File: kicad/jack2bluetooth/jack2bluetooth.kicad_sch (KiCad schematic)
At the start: 1 part, among them IC7 ESP32-WROVER-E-N16R8

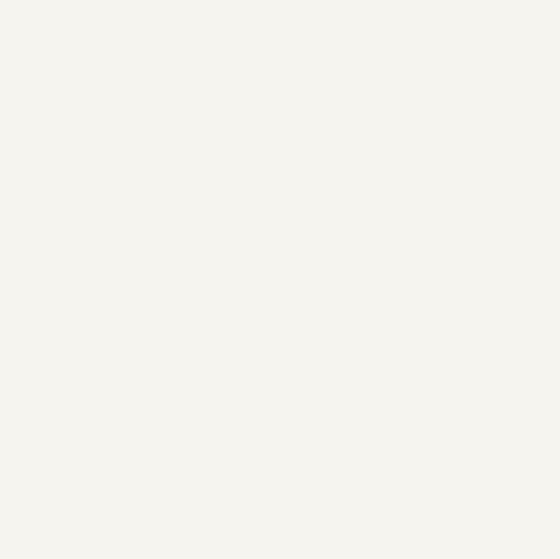
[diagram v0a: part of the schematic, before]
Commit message: doc: update datasheets
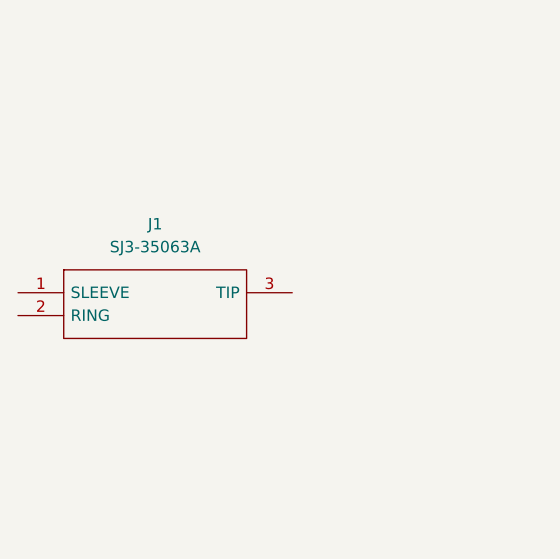
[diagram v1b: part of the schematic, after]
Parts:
- added J1: SJ3-35063A, SJ335063A, symbol SJ3-35063A:SJ3-35063A
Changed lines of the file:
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@@
+		)
+	)
+	(symbol
+		(lib_id "SJ3-35063A:SJ3-35063A")
+		(at 78.74 127 0)
+		(unit 1)
+		(exclude_from_sim no)
+		(in_bom yes)
+		(on_board yes)
+		(dnp no)
+		(fields_autoplaced yes)
+		(property "Reference" "J1"
+			(at 93.98 119.38 0)
+			(effects
+				(font
+					(size 1.27 1.27)
+				)
+			)
+		)
+		(property "Value" "SJ3-35063A"
+			(at 93.98 121.92 0)
+			(effects
+				(font
+					(size 1.27 1.27)
+				)
+			)
+		)
+		(property "Footprint" "SJ335063A"
+			(at 105.41 124.46 0)
+			(effects
+				(font
+					(size 1.27 1.27)
+				)
+				(justify left)
+				(hide yes)
+			)
+		)
+		(property "Datasheet" "https://www.sameskydevices.com/product/resource/supplyframepdf/sj3-3506x.pdf"
+			(at 105.41 127 0)
+			(effects
+				(font
+					(size 1.27 1.27)
+				)
+				(justify left)
+				(hide yes)
+			)
+		)
+		(property "Description" "3.5 mm Stereo Jack, Through Hole, 3 Conductors, 0 Internal Switches"
+			(at 78.74 127 0)
+			(effects
+				(font
+					(size 1.27 1.27)
+				)
+				(hide yes)
+			)
+		)
+		(property "Description_1" "3.5 mm Stereo Jack, Through Hole, 3 Conductors, 0 Internal Switches"
+			(at 105.41 129.54 0)
+			(effects
+				(font
+					(size 1.27 1.27)
+				)
+				(justify left)
+				(hide yes)
+			)
+		)
+		(property "Height" "6.15"
+			(at 105.41 132.08 0)
+			(effects
+				(font
+					(size 1.27 1.27)
+				)
+				(justify left)
+				(hide yes)
+			)
+		)
+		(property "Mouser Part Number" "179-SJ3-35063A"
+			(at 105.41 134.62 0)
+			(effects
+				(font
+					(size 1.27 1.27)
+				)
+				(justify left)
+				(hide yes)
+			)
+		)
+		(property "Mouser Price/Stock" "https://www.mouser.co.uk/ProductDetail/Same-Sky/SJ3-35063A?qs=IKkN%2F947nfD%2FdlMFCUr7kw%3D%3D"
+			(at 105.41 137.16 0)
+			(effects
+				(font
+					(size 1.27 1.27)
+				)
+				(justify left)
+				(hide yes)
+			)
+		)
+		(property "Manufacturer_Name" "Same Sky"
+			(at 105.41 139.7 0)
+			(effects
+				(font
+					(size 1.27 1.27)
+				)
+				(justify left)
+				(hide yes)
+			)
+		)
+		(property "Manufacturer_Part_Number" "SJ3-35063A"
+			(at 105.41 142.24 0)
+			(effects
+				(font
+					(size 1.27 1.27)
+				)
+				(justify left)
+				(hide yes)
+			)
+		)
+		(pin "1"
+		)
+		(pin "2"
+		)
+		(pin "3"
+		)
+		(instances
+			(project ""
+				(path "/4b32d186-730c-41ef-8802-f29516455534"
+					(reference "J1")
+					(unit 1)
+				)
+			)
 		)
 	)

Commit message: feat: update kicad schematic with rev3.1 updates
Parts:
- added C1, C11, C12, C14, C15, C2, C25, C27, C29, C3, C35, C38, C6, C7: 0.1uF, Capacitor_SMD:C_0805_2012Metric_Pad1.18x1.45mm_HandSolder, symbol Device:C
- added C10, C18, C20, C21, C22, C26, C28, C31, C36, C37: 10uF, Capacitor_SMD:C_0805_2012Metric_Pad1.18x1.45mm_HandSolder, symbol Device:C
- added C13, C17, C19, C30, C4, C5, C8, C9: 1uF, Capacitor_SMD:C_0805_2012Metric_Pad1.18x1.45mm_HandSolder, symbol Device:C
- added C16, C32, C33: 4.7uF, Capacitor_SMD:C_0805_2012Metric_Pad1.18x1.45mm_HandSolder, symbol Device:C
- added C23: 47nF, Capacitor_SMD:C_0805_2012Metric_Pad1.18x1.45mm_HandSolder, symbol Device:C
- added C24: 22uF, Capacitor_SMD:C_0805_2012Metric_Pad1.18x1.45mm_HandSolder, symbol Device:C
- added C34: 1u, Capacitor_SMD:C_0805_2012Metric_Pad1.18x1.45mm_HandSolder, symbol Device:C
- added D1, D2, D4, D7, D8: LED - green, LED_SMD:LED_0805_2012Metric_Pad1.15x1.40mm_HandSolder, symbol Device:LED
- added D5: PRTR5V0U2X, Package_TO_SOT_SMD:SOT-143, symbol Power_Protection:PRTR5V0U2X
- added IC1: TLV320AIC3101IRHBR, QFN50P500X500X100-33N-D, symbol TLV320AIC3101IRHBR:TLV320AIC3101IRHBR
- added IC2: BQ25619RTWR, QFN50P400X400X80-25N-D, symbol BQ25619RTWR:BQ25619RTWR
- added IC3: MCP23008T-E_SO, SOIC127P1030X265-18N, symbol MCP23008T-E_SO:MCP23008T-E_SO
- added IC4, IC5: TPS62A01PDDCR, SOT95P280X110-6N, symbol TPS62A01PDDCR:TPS62A01PDDCR
- added J10, J3, J5, J8: Conn_01x03_Pin, Connector_PinHeader_2.54mm:PinHeader_1x03_P2.54mm_Vertical, symbol Connector:Conn_01x03_Pin
- added J2: USB_C_Receptacle, Connector_USB:USB_C_Receptacle_GCT_USB4105-xx-A_16P_TopMnt_Horizontal, symbol Connector:USB_C_Receptacle
- added J4: SJ1-2503A, SJ12503A, symbol SJ1-2503A:SJ1-2503A
- added J6: Conn_01x04_Pin, Connector_PinHeader_2.54mm:PinHeader_1x04_P2.54mm_Vertical, symbol Connector:Conn_01x04_Pin
- added J7: Conn_01x02_Pin, Connector_PinHeader_2.54mm:PinHeader_1x02_P2.54mm_Vertical, symbol Connector:Conn_01x02_Pin
- added J9: Conn_01x08_Pin, Connector_PinHeader_2.54mm:PinHeader_1x08_P2.54mm_Vertical, symbol Connector:Conn_01x08_Pin
- added JP1: Jumper_3_Open, Connector_PinHeader_2.54mm:PinHeader_1x03_P2.54mm_Vertical, symbol Jumper:Jumper_3_Open
- added L1: 1uH, Inductor_SMD:L_0805_2012Metric_Pad1.05x1.20mm_HandSolder, symbol Device:L
- added L2, L3: 1uH, Inductor_SMD:L_0805_2012Metric, symbol Device:L
- added PS1: TLV75801PDBVR, SOT95P280X145-5N, symbol TLV75801PDBVR:TLV75801PDBVR
- added Q1: DMP3099L-13, SOT96P240X115-3N, symbol DMP3099L-13:DMP3099L-13
- added R1, R2, R22, R3, R37, R40: 100k, Resistor_SMD:R_0805_2012Metric_Pad1.20x1.40mm_HandSolder, symbol Device:R
- added R10, R11, R13, R14, R15, R19, R20, R21, R24, R29, R32, R34: 10k, Resistor_SMD:R_0805_2012Metric_Pad1.20x1.40mm_HandSolder, symbol Device:R
- added R23: 0, Resistor_SMD:R_0805_2012Metric_Pad1.20x1.40mm_HandSolder, symbol Device:R
- added R25: 750k, Resistor_SMD:R_0805_2012Metric_Pad1.20x1.40mm_HandSolder, symbol Device:R
- added R26, R38: 150k, Resistor_SMD:R_0805_2012Metric_Pad1.20x1.40mm_HandSolder, symbol Device:R
- added R33, R35: 499k, Resistor_SMD:R_0805_2012Metric_Pad1.20x1.40mm_HandSolder, symbol Device:R
- added R36: 200k, Resistor_SMD:R_0805_2012Metric_Pad1.20x1.40mm_HandSolder, symbol Device:R
- added R39: 300k, Resistor_SMD:R_0805_2012Metric_Pad1.20x1.40mm_HandSolder, symbol Device:R
- added R4, R7, R8, R9: 1k, Resistor_SMD:R_0805_2012Metric_Pad1.20x1.40mm_HandSolder, symbol Device:R
- added R5, R6: 5.1k, Resistor_SMD:R_0805_2012Metric_Pad1.20x1.40mm_HandSolder, symbol Device:R
- added SW1, SW2, SW3, SW4, SW6: SW_Push, Button_Switch_THT:SW_PUSH_6mm, symbol Switch:SW_Push
- added SW5: SW_SPDT, SLW-10558:SLW-105558-2A-N-D, symbol Switch:SW_SPDT
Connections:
- net GND: now reaches IC7.1 (GND_1)
- net GND: now also IC7.15 (GND_2), IC7.38 (GND_3), IC7.39 (GND_4), IC7.40 (GND_5), IC7.41 (GND_6), IC7.42 (GND_7), IC7.43 (GND_8), IC7.44 (GND_9), IC7.45 (GND_10), IC7.46 (GND_11), IC7.47 (GND_12), C10.2, C11.2, C16.1, C17.2, C22.1, C24.2, C25.2, C26.1, C27.2, C28.2, C29.2, C30.2, C32.2, C33.2, C34.1, C35.2, C36.2, C37.2, C4.2, C5.2, C6.2, C7.2, D1.1 (K), D2.1 (K), D5.1 (GND), IC1.6 (DVSS), IC2.17 (PGND_1), IC2.18 (PGND_2), IC2.25 (EP), IC3.3 (A2), IC3.4 (A1), IC3.5 (A0), IC3.9 (VSS), IC4.2 (GND), IC5.2 (GND), J10.3 (Pin_3), J2.A1 (GND), J2.A12 (GND), J2.B1 (GND), J2.B12 (GND), J2.S1 (SHIELD), J3.3 (Pin_3), J5.2 (Pin_2), J7.1 (Pin_1), J8.3 (Pin_3), J9.2 (Pin_2), J9.7 (Pin_7), JP1.3 (B), R1.1, R14.2, R2.1, R23.2, R3.1, R37.2, R40.2, R5.2, R6.1, R7.2, R8.2, SW4.1, SW5.3 (C), SW6.1
- net IO25: now reaches IC7.10 (IO25)
- net IO26: now reaches IC7.11 (IO26)
- net IO27: now reaches IC7.12 (IO27)
- net IO27: now also IC2.9 (/CE), R29.1
- net IO14: now reaches IC7.13 (IO14)
- net IO14: now also J6.1 (Pin_1)
- net IO12: now reaches IC7.14 (IO12)
- net IO12: now also J6.2 (Pin_2)
- net IO13: now reaches IC7.16 (IO13)
- net IO13: now also J6.3 (Pin_3)
- net +3.3V: now reaches IC7.2 (3V3)
- net +3.3V: now also C1.1, C2.1, C24.1, C27.1, C3.1, C37.1, C38.1, C5.1, C6.1, IC1.7 (IOVDD), L3.1, Q1.2, R19.2, R20.2, R21.2, R22.2, R24.1, R29.2, R32.2, R34.2, R38.1, SW1.2, SW2.2, SW3.2
- net IO15: now reaches IC7.23 (IO15)
- net IO15: now also J6.4 (Pin_4), J9.4 (Pin_4)
- net IO2: now reaches IC7.24 (IO2)
- net IO2: now also IC1.2 (BCLK)
- net IO0: now reaches IC7.25 (IO0)
- net IO0: now also C35.1, R21.1, SW4.2
- net IO4: now reaches IC7.26 (IO4)
- net IO4: now also IC1.3 (WCLK)
- net IO5: now reaches IC7.29 (IO5)
- net IO5: now also IC1.4 (DIN)
- net mcu_enable: now reaches IC7.3 (EN)
- net mcu_enable: now also C29.1, C30.1, R24.2, SW6.2
- net IO18: now reaches IC7.30 (IO18)
- net IO18: now also IC1.5 (DOUT)
- net IO19: now reaches IC7.31 (IO19)
- net IO19: now also IC1.9 (SDA), IC2.6 (SDA), IC3.2 (SDA), R20.1
- net IO21: now reaches IC7.33 (IO21)
- net IO21: now also IC1.8 (SCL), IC2.5 (SCL), IC3.1 (SCL), R19.1
- net RXD0: now reaches IC7.34 (RXD0)
- net RXD0: now also J3.2 (Pin_2)
- net TXD0: now reaches IC7.35 (TXD0)
- net TXD0: now also IC1.1 (MCLK), J3.1 (Pin_1)
- net IO22: now reaches IC7.36 (IO22)
- net IO23: now reaches IC7.37 (IO23)
- net IO34: now reaches IC7.6 (IO34)
- net IO34: now also J8.2 (Pin_2)
- net IO35: now reaches IC7.7 (IO35)
- net IO32: now reaches IC7.8 (IO32)
- net IO32: now also IC3.6 (~{RESET})
- net IO33: now reaches IC7.9 (IO33)
- net IO33: now also J8.1 (Pin_1)
- net GNDA: now reaches J1.1 (SLEEVE)
- net GNDA: now also C12.2, C13.2, C14.2, C15.2, C18.2, C19.2, C31.2, C34.2, IC1.17 (AVSS1), IC1.21 (DRVSS), IC1.26 (AVSS2), IC1.33 (EP), J4.1 (SLEEVE), PS1.2 (GND), R23.1, R26.2
- net jack35_right: now reaches J1.2 (RING)
- net jack35_right: now also C20.2
- net jack35_left: now reaches J1.3 (TIP)
- net jack35_left: now also C21.2
- new net: D8.2 (A), R11.2
- new net: D2.2 (A), R9.2
- new net: C22.2, IC2.23 (PMID)
- new net: IC2.3 (PMID_GOOD), R15.2
- new net: D7.1 (K), R8.1
- new net: JP1.1 (A), R10.2
- new net: D4.1 (K), R7.1
- new net: PS1.4 (FB), R25.2, R26.1
- new net: J2.A5 (CC1), R6.2
- new net: R22.1, SW5.1 (A)
- new net: D1.2 (A), R4.2
- new net: C38.2, IC3.18 (VDD)
- new net: IC4.6 (FB), R36.2, R37.1
- new net: IC5.5 (PG), R35.1
- new net: IC5.6 (FB), R39.2, R40.1
- new net: IC4.5 (PG), R33.1
- new net: J2.A6 (D+), J2.B6 (D+)
- new net: J2.A7 (D-), J2.B7 (D-)
- new net: J2.B5 (CC2), R5.1
- new net: R38.2, R39.1
- new net +1V8: C36.1, C4.1, C7.1, IC1.32 (DVDD), L2.1, R36.1
- new net +3.3VA: C12.1, C13.1, C14.1, C15.1, C18.1, C19.1, C31.1, IC1.18 (DRVDD_1), IC1.24 (DRVDD_2), IC1.25 (AVDD), PS1.5 (OUT), R25.1
- new net 1V8_SW: IC4.3 (SW), L2.2
- new net 3V3_SW: IC5.3 (SW), L3.2
- new net BAT+: C10.1, IC2.10 (BATSNS), IC2.13 (BAT_1), IC2.14 (BAT_2), J5.3 (Pin_3)
- new net BATTS: IC2.11 (TS), J5.1 (Pin_1), R13.2, R14.1
- new net BTST: C23.1, IC2.21 (BTST)
- new net HPLOUT: C21.1, IC1.19 (HPLOUT)
- new net HPROUT: C20.1, IC1.23 (HPROUT)
- new net IO16: J9.5 (Pin_5)
- new net IO17: J9.3 (Pin_3)
- new net IO3: J9.6 (Pin_6)
- new net IO36: IC3.8 (INT)
- new net IO39: IC2.7 (/INT), R32.1
- new net IO_EXP_0: C2.2, IC3.10 (GP0), R2.2, SW2.1
- new net IO_EXP_1: C1.2, IC3.11 (GP1), R1.2, SW1.1
- new net IO_EXP_2: C3.2, IC3.12 (GP2), R3.2, SW3.1
- new net IO_EXP_3: C25.1, IC3.13 (GP3), SW5.2 (B)
- new net IO_EXP_4: D4.2 (A), IC3.14 (GP4)
- new net IO_EXP_5: D7.2 (A), IC3.15 (GP5)
- new net IO_EXP_6: IC3.16 (GP6), Q1.1, R34.1
- new net IO_EXP_7: IC1.31 (~{RESET}), IC3.17 (GP7)
- new net LINE2L: C9.2, IC1.14 (MIC2L/LINE2L/MICDET)
- new net LINE2R: C8.2, IC1.16 (MIC2R/LINE2R)
- new net PSEL: IC2.2 (PSEL), JP1.2 (C)
- new net REGN: C16.2, IC2.22 (REGN), R10.1, R13.1, R15.1
- new net STAT: D8.1 (K), IC2.4 (STAT)
- new net SW: C23.2, IC2.19 (SW_1), L1.1
- new net SYSTEM: C26.2, C28.1, C32.1, C33.1, IC2.15 (SYS_1), IC2.16 (SYS_2), IC4.1 (EN), IC4.4 (VIN), IC5.1 (EN), IC5.4 (VIN), J10.2 (Pin_2), L1.2, PS1.1 (IN), PS1.3 (EN), R11.1, R33.2, R35.2, R9.1
- new net USB_DN: D5.2 (I/O1)
- new net USB_DP: D5.3 (I/O2)
- new net VCC: C17.1, D5.4 (VCC), IC2.1 (VAC), IC2.24 (VBUS), J10.1 (Pin_1), J2.A4 (VBUS), J2.A9 (VBUS), J2.B4 (VBUS), J2.B9 (VBUS), R4.1
- new net jack25_left: C9.1, J4.2 (TIP_1), J4.3 (TIP_2)
- new net jack25_right: C8.1, J4.4 (RING)
- new net lcd_blk: J9.1 (Pin_1), J9.8 (Pin_8), Q1.3
- new net nQON: C11.1, IC2.12 (/QON), J7.2 (Pin_2)
- no-connect marks 0 -> 33
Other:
- note added: "Audio Codec"
- note added: "Battery Temperature Sensing"
- note added: "Boot"
- note added: "Boot Config: 1 ON - Boot from UART 2 OFF - Boot from SPI"
- note added: "Connect inputs"
- note added: "Connect outputs"
- note added: "Connexions with MCU"
- note added: "Control Buttons"
- note added: "ESD protection"
- note added: "I2C"
- note added: "I2C address is 0x20"
- note added: "I2S"
- note added: "IO expander - user interface"
- note added: "IOs exp"
- note added: "JTAG"
- note added: "LDO - Analog Regulator"
- note added: "LED"
- note added: "MCU : ESP32-C6-WROOM-1-N8"
- note added: "On/Off button"
- note added: "PMIC"
- note added: "PMIC (BQ25619)"
- note added: "PSEL input current limit 1 : 500mA USB UDP (default) 3 : 2.4A Adapter"
- note added: "Reset button Should be Hidden"
- note added: "SCL : SPI SDA : SPI RES : Reset DC : Data or Command mode CS : CS (low to select) BLK : back light control (PWM)"
- note added: "SPI Screen / JTAG"
- note added: "Switching Regulators (1.8V and 3.3V)"
- note added: "UART Connectors"
- note added: "USB-C Connector"
- note added: "Uart"
- note added: "Vsystem led"
- note added: "buttons"
- note added: "charging enable"
- note added: "codec"
- note added: "external power led"
- note added: "internal power led"
- note added: "jack 2.5mm"
- note added: "jack 3.5mm"
- note added: "leds"
- note added: "with a 2mm header, this should be compatible with a JST PH2.0 female connector !!!When soldering, Carefull with direction!!!!!"
- moved on the sheet: IC7, J1

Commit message: feat: update kicad schematic with latest Rev3.1 updates
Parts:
- removed D5: PRTR5V0U2X, Package_TO_SOT_SMD:SOT-143, symbol Power_Protection:PRTR5V0U2X
- removed J8: Conn_01x03_Pin, Connector_PinHeader_2.54mm:PinHeader_1x03_P2.54mm_Vertical, symbol Connector:Conn_01x03_Pin
- added C39, C40, C41, C42: 1uF, Capacitor_SMD:C_0805_2012Metric_Pad1.18x1.45mm_HandSolder, symbol Device:C
- added C43: 100uF, Capacitor_SMD:C_0805_2012Metric_Pad1.18x1.45mm_HandSolder, symbol Device:C
- added D3: 1N5819, Diode_THT:D_DO-41_SOD81_P10.16mm_Horizontal, symbol Diode:1N5819
- added D5: SMF5V0A, Diode_SMD:D_SMF, symbol Diode:SMF5V0A
- added F1, F2: Polyfuse, symbol Device:Polyfuse
- added Q2, Q3: BC846, Package_TO_SOT_SMD:SOT-23, symbol Transistor_BJT:BC846
- added R12, R16, R17, R18: 0, Resistor_SMD:R_0805_2012Metric_Pad1.20x1.40mm_HandSolder, symbol Device:R
- added SW7: SW_SPDT, SLW-10558:SLW-105558-2A-N-D, symbol Switch:SW_SPDT
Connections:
- net +3.3V: now also C35.2, SW4.1; no longer R21.2
- net BAT+: now also C43.1, F2.2; no longer J5.3 (Pin_3)
- net GND: now also R21.1, C43.2, D5.2 (A2), Q2.2 (E), Q3.2 (E); no longer C35.2, SW4.1
- net GNDA: now also C39.1, C40.1, C41.1, C42.1
- net IO0: now also Q2.3 (C); no longer C35.1, R21.1, SW4.2
- net IO2: now also Q3.3 (C)
- net LINE2L: now also C40.2, R16.1; no longer C9.2
- net LINE2R: now also C39.2, R12.1; no longer C8.2
- net SYSTEM: now also SW7.1 (A); no longer IC2.15 (SYS_1), IC2.16 (SYS_2)
- net VCC: now also F1.2; no longer J2.A4 (VBUS), J2.A9 (VBUS), J2.B4 (VBUS), J2.B9 (VBUS)
- net jack35_left: now also C42.2, R18.1; no longer C21.2
- net jack35_right: now also C41.2, R17.1; no longer C20.2
- net at J2.A6 (D+): no longer J2.B6 (D+)
- net at J2.A7 (D-): no longer J2.B7 (D-)
- new net: D3.1 (K), F1.1
- new net: C8.2, R12.2
- new net: C35.1, Q2.1 (B), Q3.1 (B), R21.2, SW4.2
- new net: C9.2, R16.2
- new net: F2.1, J5.3 (Pin_3)
- new net: C21.2, R18.2
- new net: C20.2, R17.2
- new net PMIC_SYSTEM: IC2.15 (SYS_1), IC2.16 (SYS_2), SW7.2 (B)
- new net usb_vbus: D3.2 (A), D5.1 (A1), J2.A4 (VBUS), J2.A9 (VBUS), J2.B4 (VBUS), J2.B9 (VBUS)
- no-connect marks 33 -> 38
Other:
- note added: "SMDH1210B075TF"
- note added: "TVS diode protect against ESD Shottky diode protect against reverse current Polyfuse protect against short circuit (current > 500mA)"
- note added: "This 2mm header, should be compatible with a JST PH2.0 female connector !!!When soldering, Carefull with direction!!!!!"
- note removed: "ESD protection"
- note removed: "with a 2mm header, this should be compatible with a JST PH2.0 female connector !!!When soldering, Carefull with direction!!!!!"
- moved on the sheet: C10, C20, C21, C35, C8, C9, J5, R21, R5, R6, SW4

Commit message: feat: add test points to schematic
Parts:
- added J8: Conn_01x02_Pin, symbol Connector:Conn_01x02_Pin
- added TP1, TP10, TP11, TP12, TP13, TP14, TP15, TP16, TP17, TP18, TP19, TP2, TP20, TP21, TP22, TP23, TP24, TP25, TP26, TP27, TP28, TP29, TP3, TP30, TP31, TP32, TP33, TP34, TP4, TP5, TP6, TP7, TP8, TP9: TestPoint, symbol Connector:TestPoint
- IC1: footprint QFN50P500X500X100-33N-D -> (none)
- IC2: footprint QFN50P400X400X80-25N-D -> (none)
- IC3: footprint SOIC127P1030X265-18N -> (none)
- IC4, IC5: footprint SOT95P280X110-6N -> (none)
- IC7: footprint ESP32WROVEREN16R8 -> (none)
- J1: footprint SJ335063A -> (none)
- J4: footprint SJ12503A -> (none)
- PS1: footprint SOT95P280X145-5N -> (none)
- Q1: footprint SOT96P240X115-3N -> (none)
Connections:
- net SW is gone; now on net TP_SW: C23.2, IC2.19 (SW_1), L1.1
- net +1V8: now also TP5.1
- net +3.3V: now also TP4.1
- net +3.3VA: now also TP3.1
- net BAT+: now also TP17.1
- net BATTS: now also TP15.1
- net GND: now also TP6.1
- net GNDA: now also TP7.1
- net HPLOUT: now also TP32.1
- net HPROUT: now also TP33.1
- net IO18: now also TP27.1
- net IO19: now also J8.2 (Pin_2), TP12.1, TP29.1
- net IO2: now also TP24.1
- net IO21: now also J8.1 (Pin_1), TP11.1, TP28.1
- net IO27: now also TP14.1
- net IO36: now also IC7.4 (SENSOR_VP)
- net IO39: now also IC7.5 (SENSOR_VN), TP13.1
- net IO4: now also TP25.1
- net IO5: now also TP26.1
- net IO_EXP_7: now also TP34.1
- net LINE2L: now also TP30.1
- net LINE2R: now also TP31.1
- net PMIC_SYSTEM: now also TP18.1
- net PSEL: now also TP8.1
- net REGN: now also TP21.1
- net STAT: now also TP10.1
- net SYSTEM: now also TP2.1
- net TXD0: now also TP23.1
- net VCC: now also TP1.1
- net nQON: now also TP16.1
- net TP_SW: now reaches IC2.20 (SW_2)
- net TP_SW: now also TP19.1
- net TP_PMID: now reaches C22.2, IC2.23 (PMID)
- net TP_PMID: now also TP22.1
- net PMID_GOOD: now reaches IC2.3 (PMID_GOOD), R15.2
- net PMID_GOOD: now also TP9.1
- net BTST renamed TP_BTST
- net TP_BTST: now also TP20.1
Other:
- note added: "Test points audio codec"
- note added: "Test points pmic"
- note added: "Test points power"
- moved on the sheet: F2, J10, J5, J6, J9

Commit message: feat: remove warnings in ERC errors and warnings in schematic. refresh layout
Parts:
- removed D5: SMF5V0A, Diode_SMD:D_SMF, symbol Diode:SMF5V0A
- added D5: SMF5V0A-E3-08, LIB_SMF5V0A-E3-08:SMF5V0AE308, symbol SMF5V0A-E3-08:SMF5V0A-E3-08
- D3: footprint Diode_THT:D_DO-41_SOD81_P10.16mm_Horizontal -> Diode_SMD:D_SOD-123
- F1, F2: footprint (none) -> Fuse:Fuse_1210_3225Metric_Pad1.42x2.65mm_HandSolder
- IC1: footprint (none) -> TLV320AIC3101IRHBR:QFN50P500X500X100-33N-D
- IC2: footprint (none) -> BQ25619RTWR:QFN50P400X400X80-25N-D
- IC3: footprint (none) -> LIB_MCP23008T-E_SO:SOIC127P1030X265-18N
- IC4, IC5: footprint (none) -> TPS62A01PDDCR:SOT95P280X110-6N
- IC7: footprint (none) -> ESP32-WROVER-E-N16R8:ESP32WROVEREN16R8
- J1: footprint (none) -> LIB_SJ3-35063A:SJ335063A
- J4: footprint (none) -> LIB_SJ1-2503A:SJ12503A
- J8: footprint (none) -> Connector_PinHeader_2.00mm:PinHeader_1x02_P2.00mm_Vertical
- PS1: footprint (none) -> TLV75801PDBVR:SOT95P280X145-5N
- Q1: footprint (none) -> DMP3099L-13:SOT96P240X115-3N
- TP1, TP10, TP11, TP12, TP13, TP14, TP15, TP16, TP17, TP18, TP19, TP2, TP20, TP21, TP22, TP23, TP24, TP25, TP26, TP27, TP28, TP29, TP3, TP30, TP31, TP32, TP33, TP34, TP4, TP5, TP6, TP7, TP8, TP9: footprint (none) -> TestPoint:TestPoint_Pad_D1.0mm
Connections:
- net IO16 is gone; now on net IO23: J9.5 (Pin_5)
- net IO17 is gone; now on net IO26: J9.3 (Pin_3)
- net IO3 is gone; now on net IO22: J9.6 (Pin_6)
- net GND: now also D5.1
- net IO15: no longer J9.4 (Pin_4)
- net IO25: now also J9.4 (Pin_4)
- net usb_vbus: now also D5.2
- no-connect marks 38 -> 37
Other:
- moved on the sheet: C2, C3, D1, D2, D3, D4, D7, J1, J4, R1, R24, R3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
